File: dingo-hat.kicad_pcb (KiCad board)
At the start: 2 copper layers, 65 x 56 mm, 91 parts, among them J1 LiPo-Power, J10 PJ-038AH, J11 Bypass-Power, J12 Chassis-Out, J13 i2c_display, J14 NEOPIXEL, J15 MPU-9250, J16 i2c_display_1, J2 Raspberry_Pi_2_3, J24 M2.5_Mount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

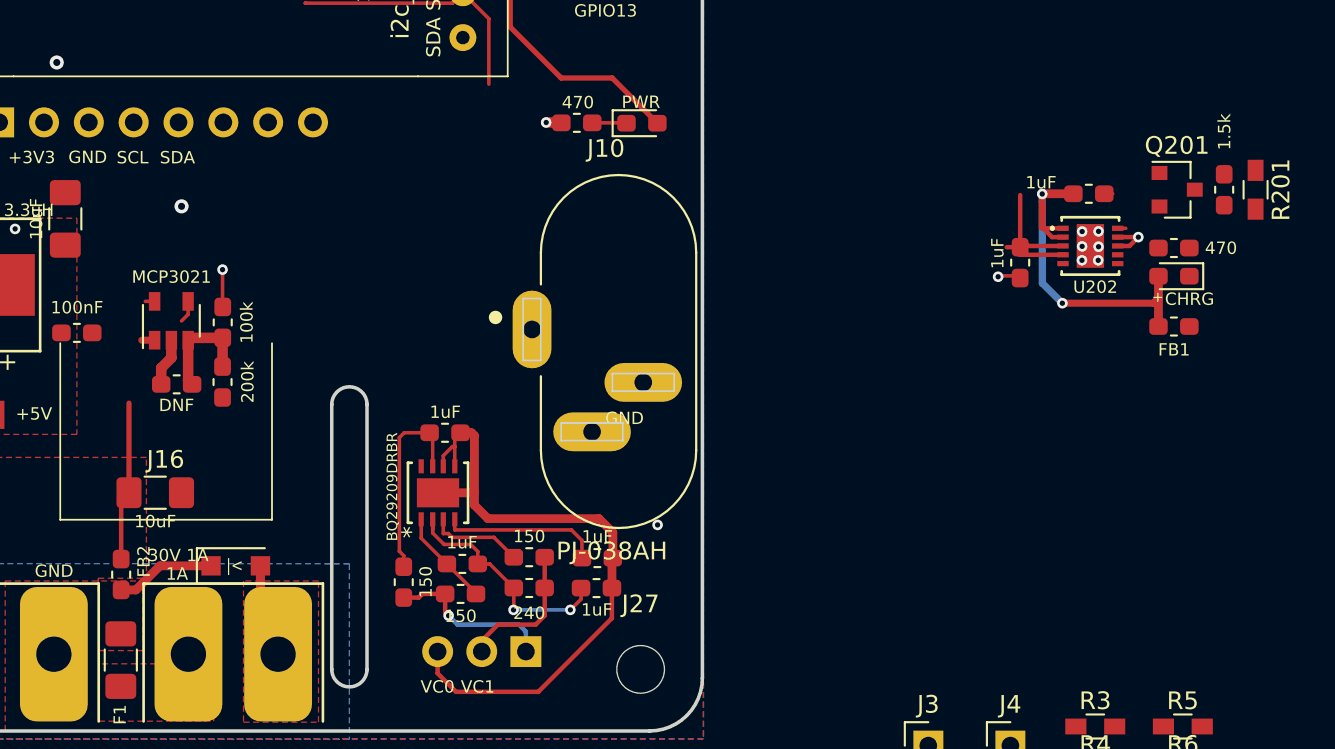
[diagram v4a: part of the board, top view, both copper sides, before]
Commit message: Compactifying the balance circuit, making heaps of space.
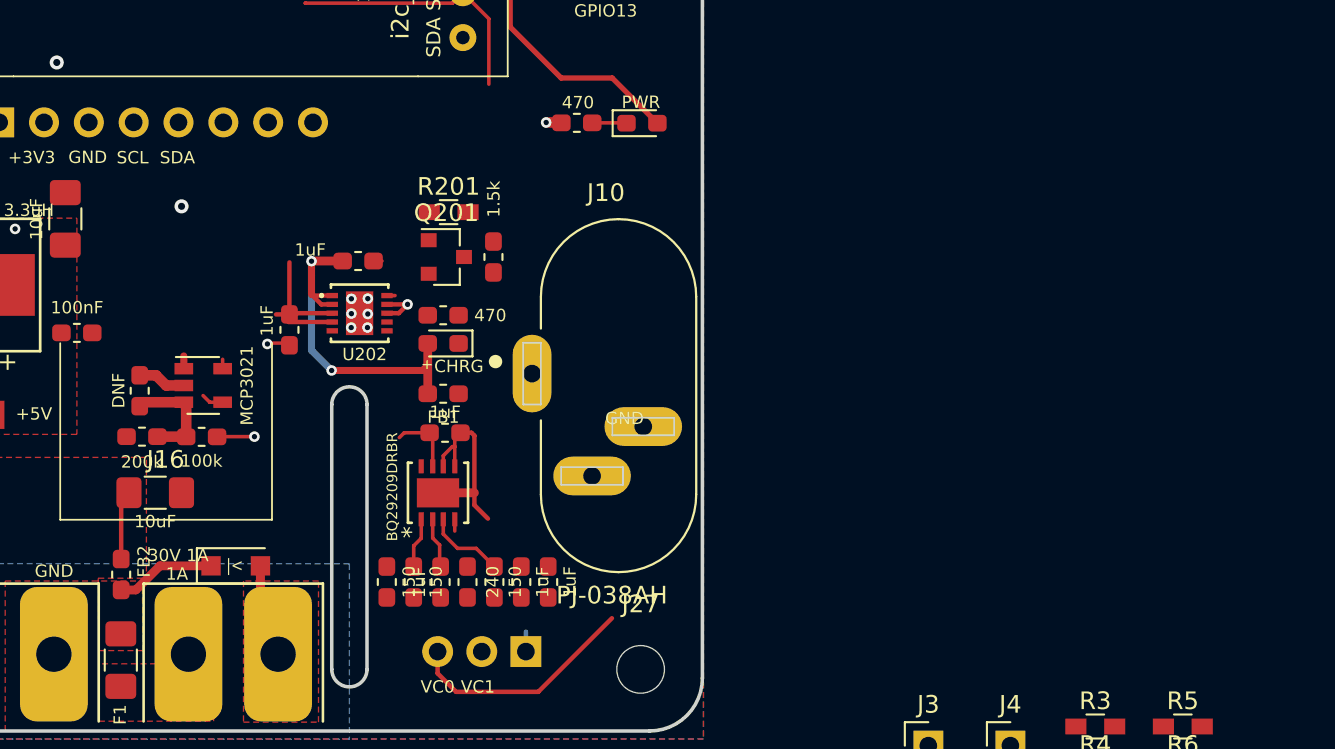
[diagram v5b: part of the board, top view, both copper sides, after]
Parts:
- moved R201 45.7 mm to (150.6, 70.1), turned to 0 degrees
- moved C202 41.6 mm to (145.5, 72.9)
- moved D201 41.6 mm to (150.3, 77.5)
- moved FB1 41.6 mm to (150.3, 80.4)
- moved R202 41.6 mm to (150.3, 75.9)
- moved C204 41.6 mm to (141.6, 76.8)
- moved Q201 41.6 mm to (150.5, 72.6)
- moved R204 41.6 mm to (153.2, 72.6)
- moved U202 41.6 mm to (145.6, 75.8)
- moved R13 6.59 mm to (136.6, 82.8), turned to 180 degrees
- moved R12 5.51 mm to (133.2, 82.8), turned to 0 degrees
- moved C207 4.52 mm to (154.7, 91.1), turned to 270 degrees
- moved U1 4.08 mm to (136.7, 79.9), turned to 0 degrees
- moved R205 3.51 mm to (151.7, 91.1), turned to 90 degrees
- moved C206 2.76 mm to (156.3, 91.1), turned to 90 degrees
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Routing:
- net /VC0: track 41.9 -> 25.3 mm
- net Net-(C205-Pad2): track 13.6 -> 2.87 mm, vias 2 -> 0
- net /VC2: track 9.63 -> 1.13 mm, vias 1 -> 0
- net Net-(C207-Pad1): track 9.06 -> 0.67 mm
- net /VC1: track 8.07 -> 0.61 mm
- net Net-(C208-Pad1): track 11.3 -> 3.87 mm
- net /BatterySupply: track 18.5 -> 13.4 mm
- net Net-(C205-Pad1): track 5.52 -> 2.86 mm
- net Net-(R206-Pad1): track 5.36 -> 4.50 mm
- net GND: vias 41 -> 40

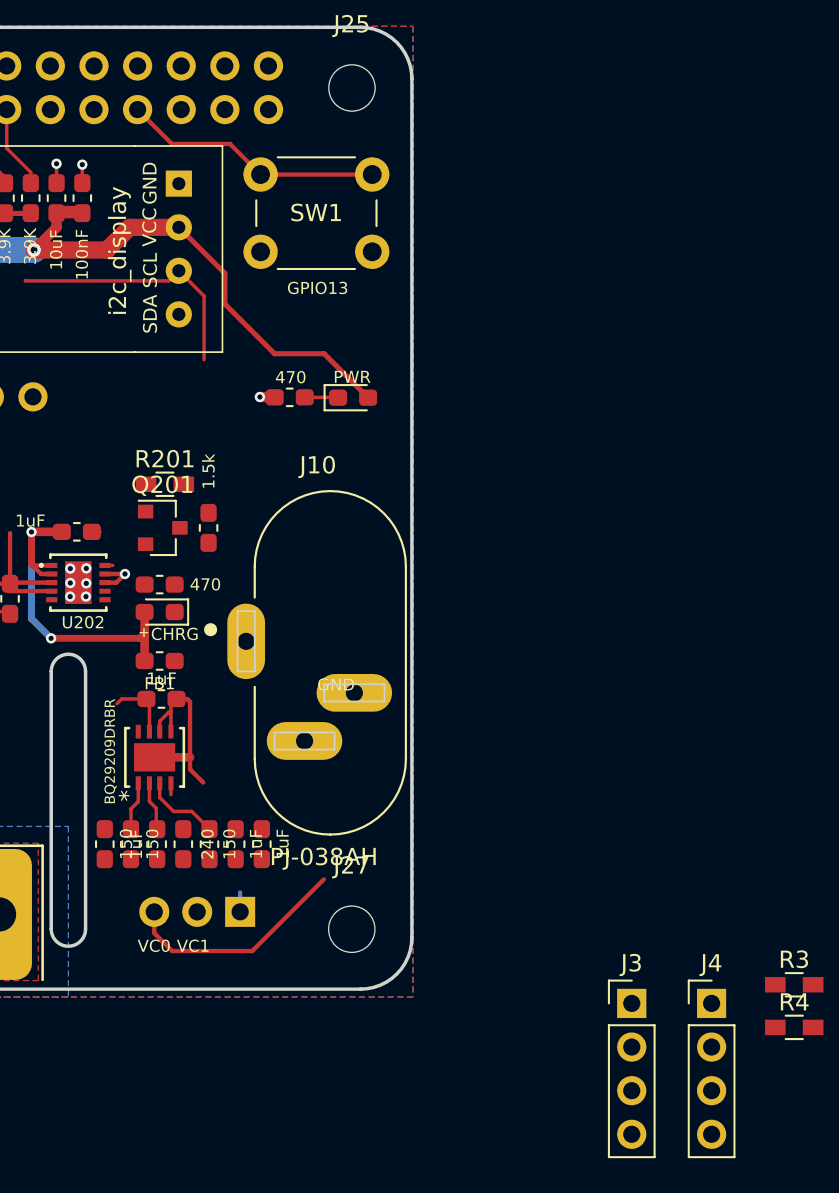
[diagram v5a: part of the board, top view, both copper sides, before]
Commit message: Most things in place, thinking about adding power button, other buttons.
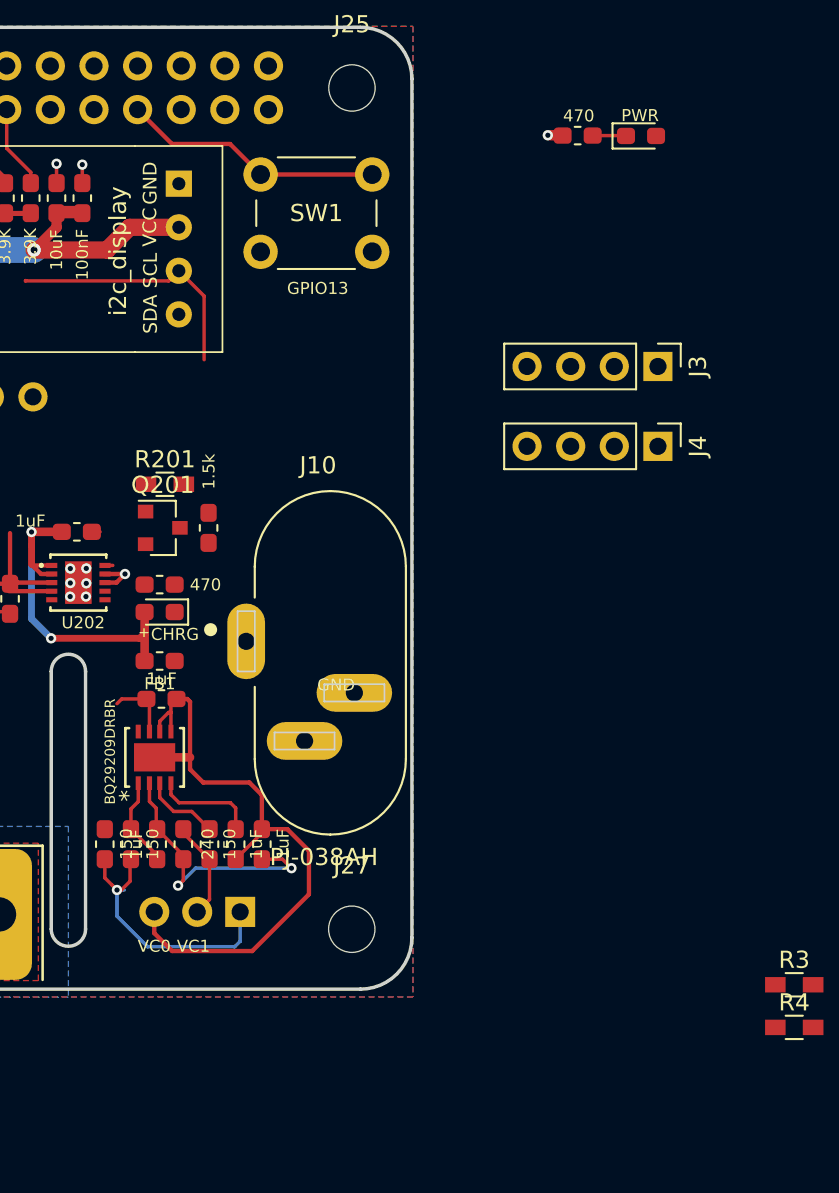
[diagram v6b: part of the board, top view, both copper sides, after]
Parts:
- moved J3 37.1 mm to (179.3, 63.2), turned to 270 degrees
- moved J4 32.6 mm to (179.3, 67.9), turned to 270 degrees
- moved D1 22.7 mm to (178.3, 49.8)
- moved R1 22.7 mm to (174.7, 49.8)
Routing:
- net +5V: track 100.3 -> 84.1 mm
- net /VC0: track 25.3 -> 40.7 mm
- net /VC2: track 1.13 -> 16.1 mm, vias 0 -> 1
- net Net-(C205-Pad2): track 2.87 -> 15.9 mm, vias 0 -> 2
- net /VC1: track 0.61 -> 6.36 mm
- net Net-(C207-Pad1): track 0.67 -> 5.99 mm
- net Net-(C205-Pad1): track 2.86 -> 5.24 mm

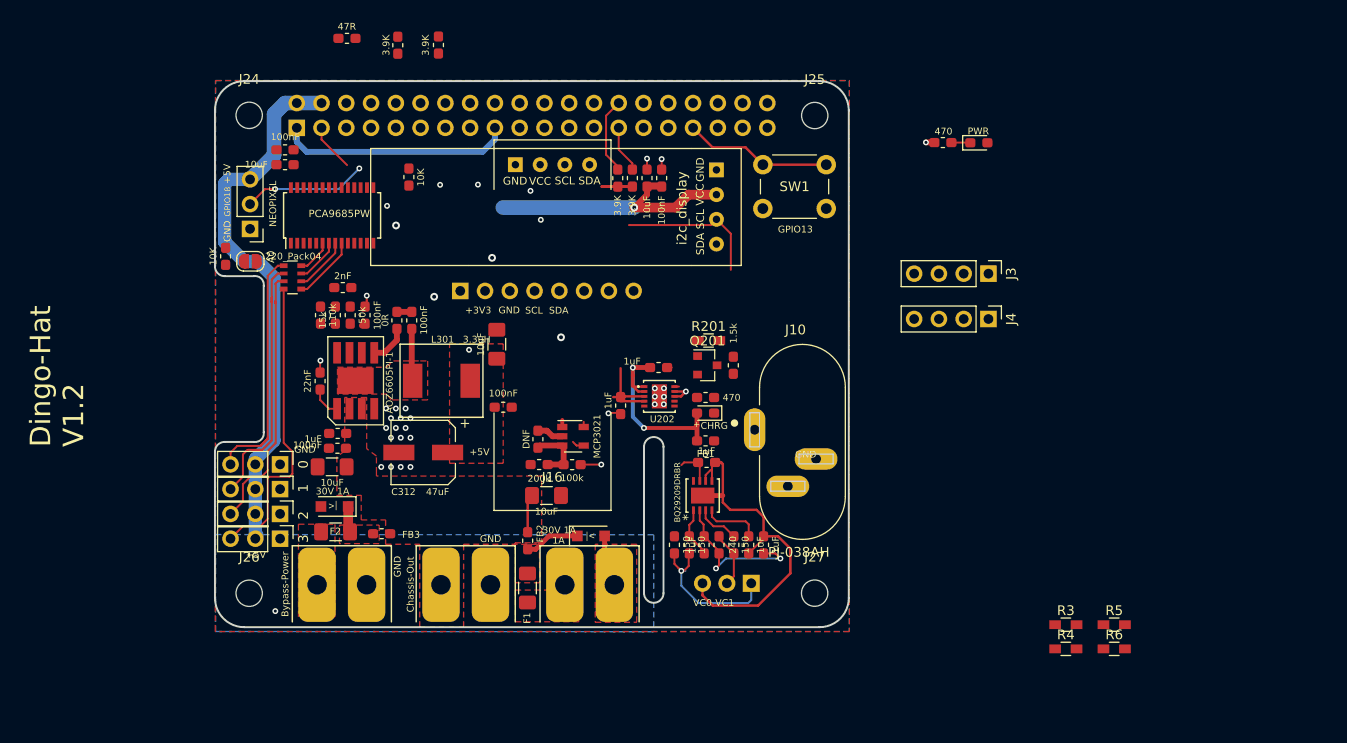
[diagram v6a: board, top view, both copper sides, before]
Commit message: Routed with dual oled
Single Ultrasonic has made it back.  Yay!
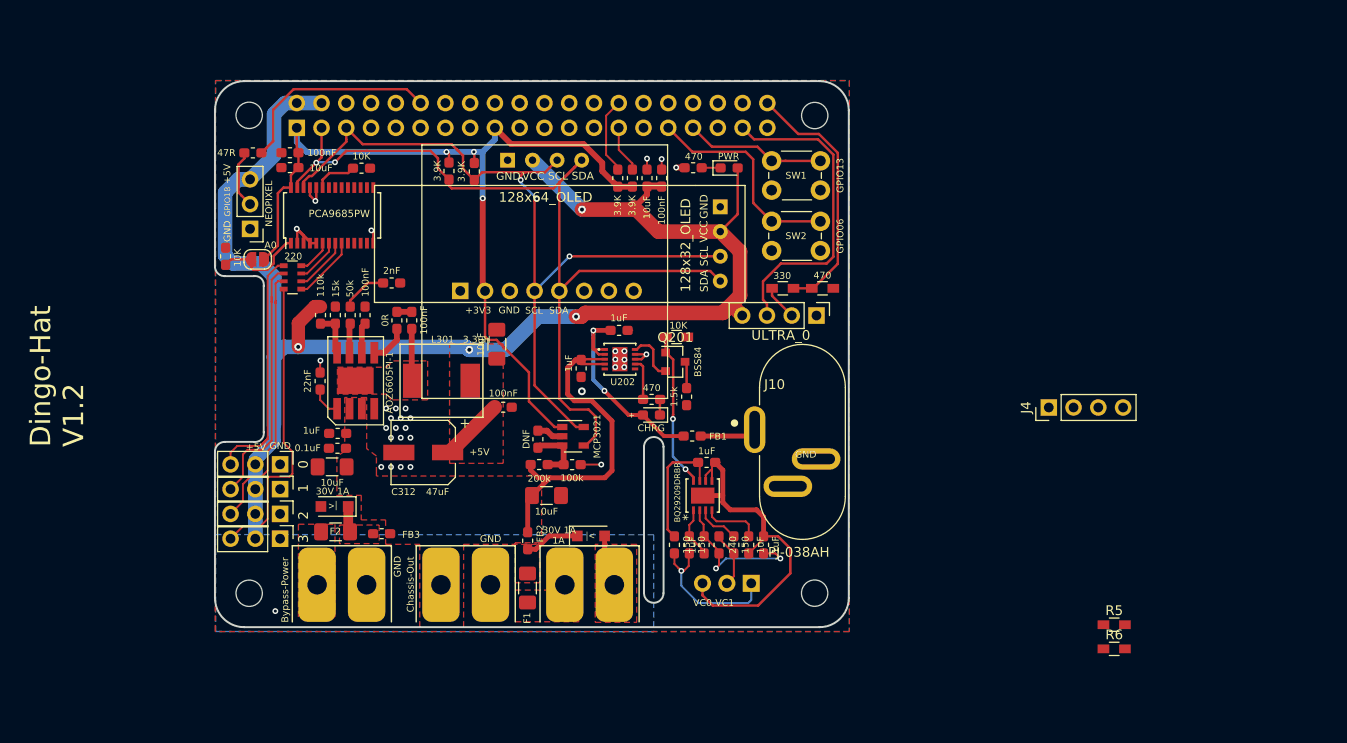
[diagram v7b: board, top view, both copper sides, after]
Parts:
- removed G3: LCA2020Logo.2, libs:logo.LCA.2020.2
- added SW2: GPIO06, libs:SW_PUSH_4.5mm, F.Cu at (157.1, 57.9)
- C306: value 100nF -> 0.1uF
- J13: value i2c_display -> 128x32_OLED
- J16: value i2c_display_1 -> 128x64_OLED; footprint libs:0.91 OLED -> libs:128x64_OLED
- RN1: value 220_Pack04 -> 220
- SW1: footprint Button_Switch_THT:SW_PUSH_6mm -> libs:SW_PUSH_4.5mm
- moved G2 64.7 mm to (68.9, 43.6)
- moved G1 64.7 mm to (48.5, 59.8)
- moved G4 64.7 mm to (48.7, 46.2)
- moved G5 64.6 mm to (48.7, 46.2)
- moved R3 45.1 mm to (158.2, 64.8)
- moved R4 44.6 mm to (162.3, 64.8)
- moved D1 25.7 mm to (152.7, 52.4)
- moved R1 25.7 mm to (149.0, 52.4)
- moved J3 18.1 mm to (161.7, 67.5)
- moved R2 15.2 mm to (103.9, 50.9)
- moved R10 13.9 mm to (124.0, 52.7)
- moved R11 13.5 mm to (126.6, 52.8)
- moved J4 11.0 mm to (185.5, 77.0), turned to 90 degrees
- moved R204 5.77 mm to (148.4, 75.9)
- moved C204 5.56 mm to (137.6, 73.0)
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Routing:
- net /SDA_3.3: track 6.18 -> 89.9 mm, vias 0 -> 2
- net +5V: track 84.1 -> 164.1 mm, vias 2 -> 4
- net /SCL_3.3: track 15.5 -> 83.9 mm, vias 0 -> 3
- net +3V3: track 33.8 -> 91.4 mm, vias 0 -> 3
- net /GPIO26: track 0.00 -> 32.8 mm
- net /GPIO21: track 0.00 -> 26.3 mm
- net /BatterySupply: track 13.4 -> 36.6 mm
- net /GPIO06: track 0.00 -> 22.2 mm
- net /GPIO18: track 0.00 -> 21.5 mm
- net /LiPoBatteryMgmt/BalOUT: track 0.00 -> 16.0 mm, vias 0 -> 2
- net /A0: track 0.00 -> 9.81 mm
- net GND: track 24.8 -> 33.7 mm, vias 40 -> 33
- net Net-(C208-Pad1): track 3.87 -> 12.6 mm
- net Net-(J14-Pad2): track 12.7 -> 5.99 mm, vias 2 -> 0
- net Net-(FB1-Pad2): track 0.00 -> 5.80 mm
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
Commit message: Added logos
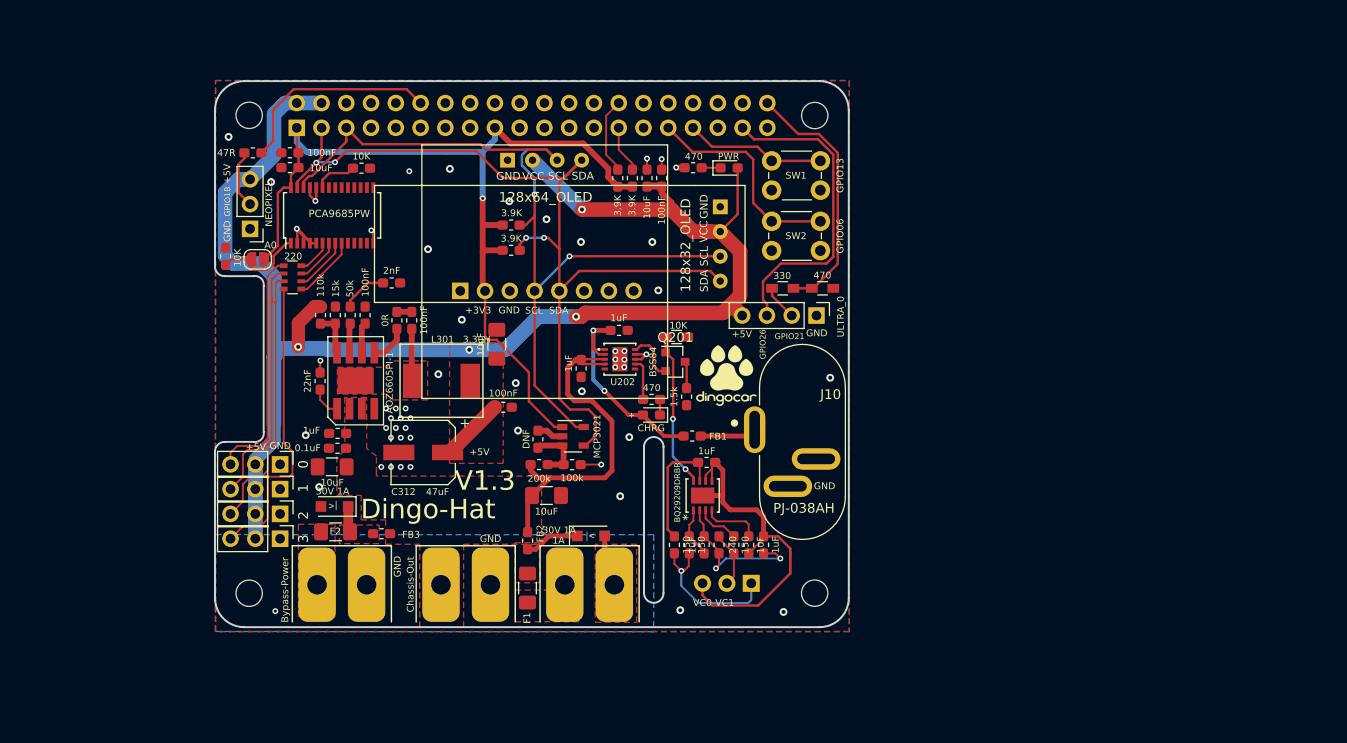
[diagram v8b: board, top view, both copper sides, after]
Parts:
- removed J4: ULTRA_1, Pin_Headers:Pin_Header_Straight_1x04_Pitch2.54mm
- removed R5: 330, Resistors_SMD:R_0603_HandSoldering
- removed R6: 470, Resistors_SMD:R_0603_HandSoldering
- added G***: LOGO, libs:logo.dingocar, B.Cu at (160.7, 76.7)
- added G***: LOGO, libs:logo.dingocar, F.Cu at (152.5, 73.7)
- added G***: LOGO, libs:logo.HeartOfPluto2, B.Cu at (139.8, 81.6)
- added G***: LOGO, libs:logo.superhouse, B.Cu at (122.2, 87.2)
- added G***: LOGO, libs:logo.pc, B.Cu at (151.1, 84.3)
- moved G1 63.6 mm to (111.0, 71.8)
- moved G4 62.8 mm to (110.2, 58.9)
- moved G5 62.8 mm to (110.2, 58.9)
- moved G2 62.8 mm to (130.4, 56.3)
- moved R10 10.3 mm to (130.4, 60.9), turned to 0 degrees
- moved R11 6.66 mm to (130.4, 58.3), turned to 0 degrees
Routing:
- net /SCL_3.3: track 83.9 -> 88.9 mm, vias 3 -> 2
- net /SDA_3.3: track 89.9 -> 93.5 mm, vias 2 -> 4
- net +3V3: track 91.4 -> 93.2 mm, vias 3 -> 1
- net GND: vias 33 -> 55
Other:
- board text added: "Designed by Bob Powers & John Spencer © 2019 Bob Powers, John Spencer License TAPR OHL v1.0"
- board text added: "Dingo-Hat"
- board text added: "GPIO21"
- board text added: "GPIO26"
- board text added: "V1.3"
- board text removed: "Designed by John Spencer © 2018 John Spencer License TAPR OHL v1.0"
- board text removed: "Dingo-Hat V1.2"
